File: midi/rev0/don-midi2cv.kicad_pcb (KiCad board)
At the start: 4 copper layers, 65.8 x 128.5 mm, 113 parts, among them J1 DIN-5_180degree, J10 CV1, J11 CV2, J12 VEL1, J13 VEL2, J2 Conn_02x03_Odd_Even, J3 Conn_02x08_Odd_Even, J5 UART, J7 MIDICLK, J8 GATE1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

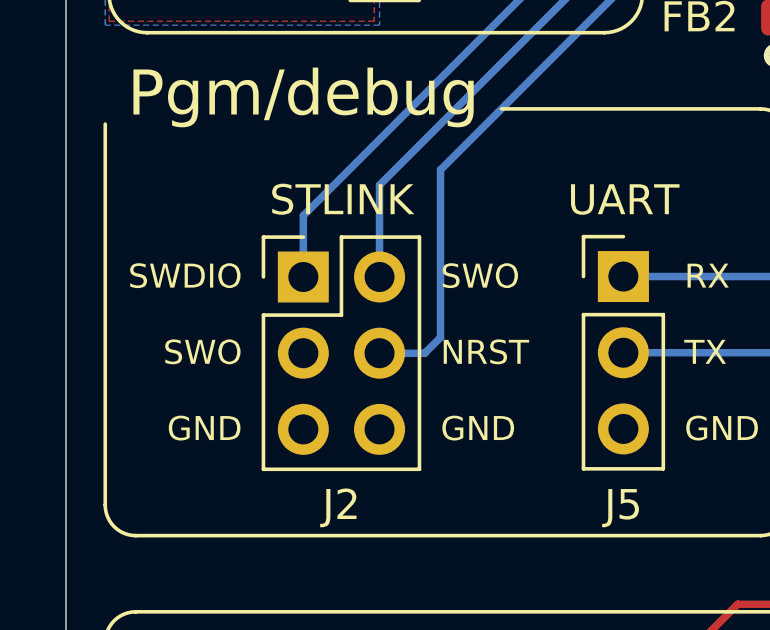
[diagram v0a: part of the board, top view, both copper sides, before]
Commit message: midi: first prototype populated
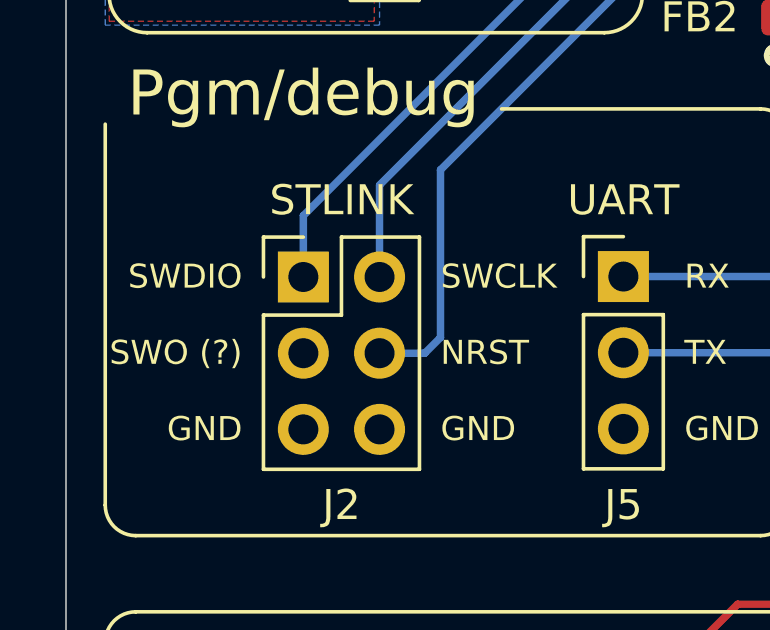
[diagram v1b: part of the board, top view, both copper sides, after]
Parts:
- C20, C21, C22, C23: value .1u -> 100n
- R30, R31, R32, R33, R34, R35, R36: value 0R -> 0
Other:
- board text added: "SWCLK"
- board text added: "SWO (?)"
- board text removed: "SWO"
